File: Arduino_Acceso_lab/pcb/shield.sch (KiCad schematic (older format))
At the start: 34 parts, among them K1 RELAY_C, K2 RELAY_C, P1 Power, P10 Sensor1, P11 Sensor2, P12 Luz1, P13 Luz2, P2 Analog, P3 Digital, P4 Digital, P5 modulo esp8266, P6 fuente, P7 buzzer 1, P8 buzzer 2, P9 Timer RTC, Q1 2N2222, Q2 2N2222, U1 LM2576

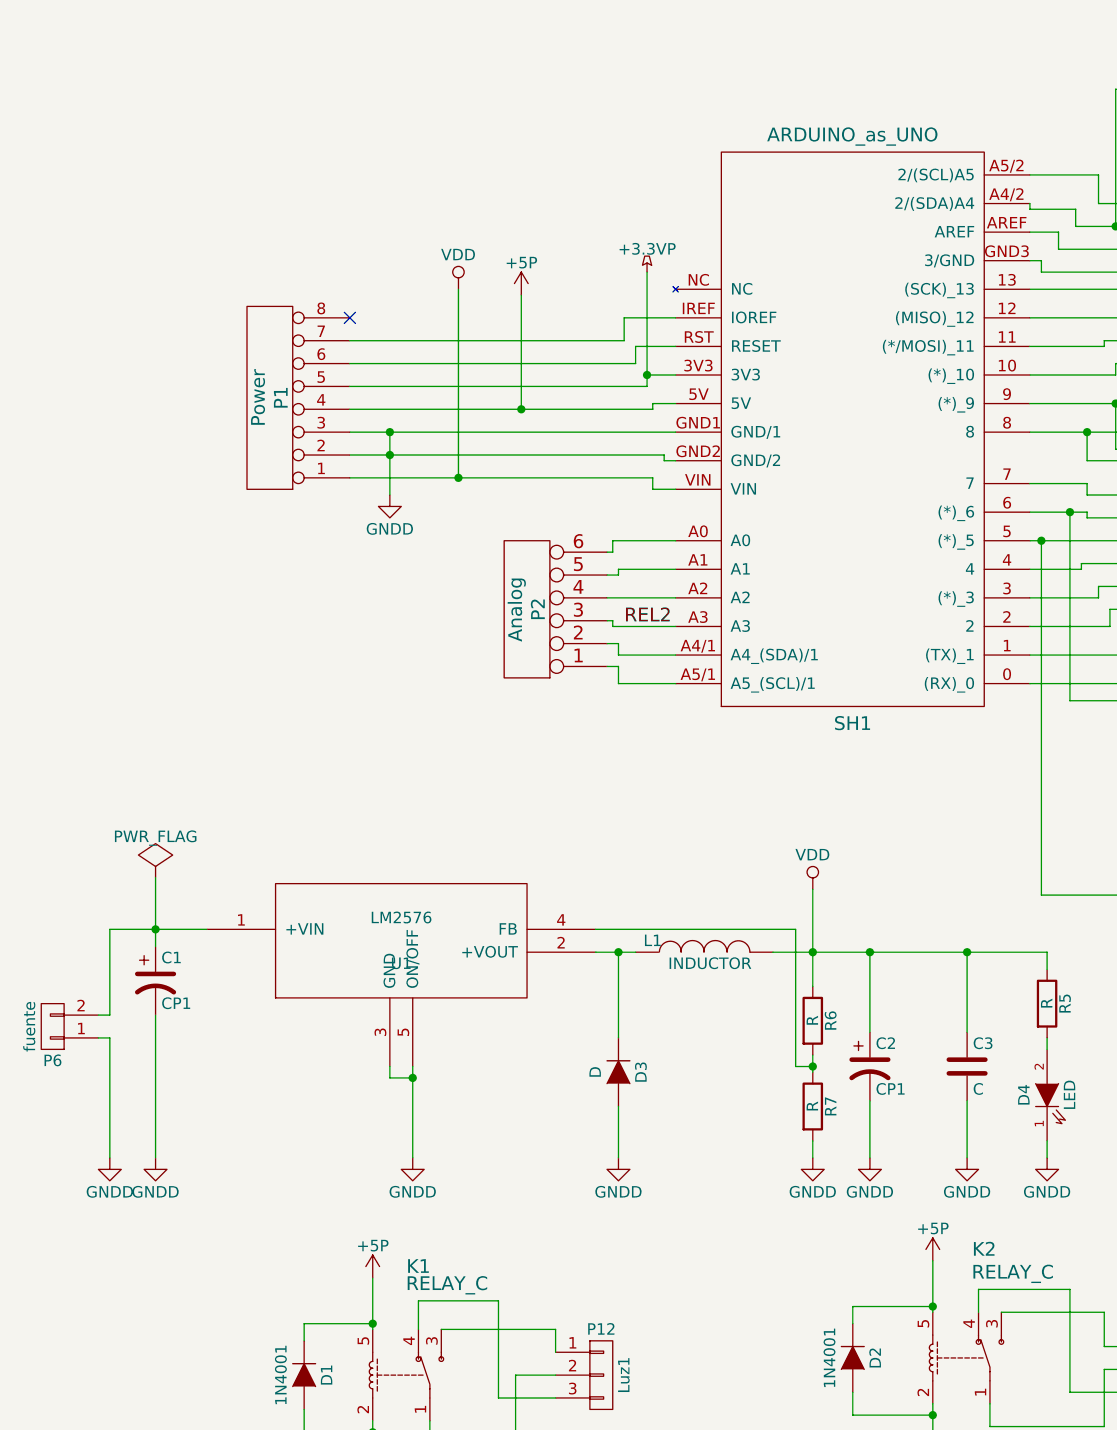
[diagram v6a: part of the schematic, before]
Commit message: Agrego avances en el PCB de Acceso Lab.
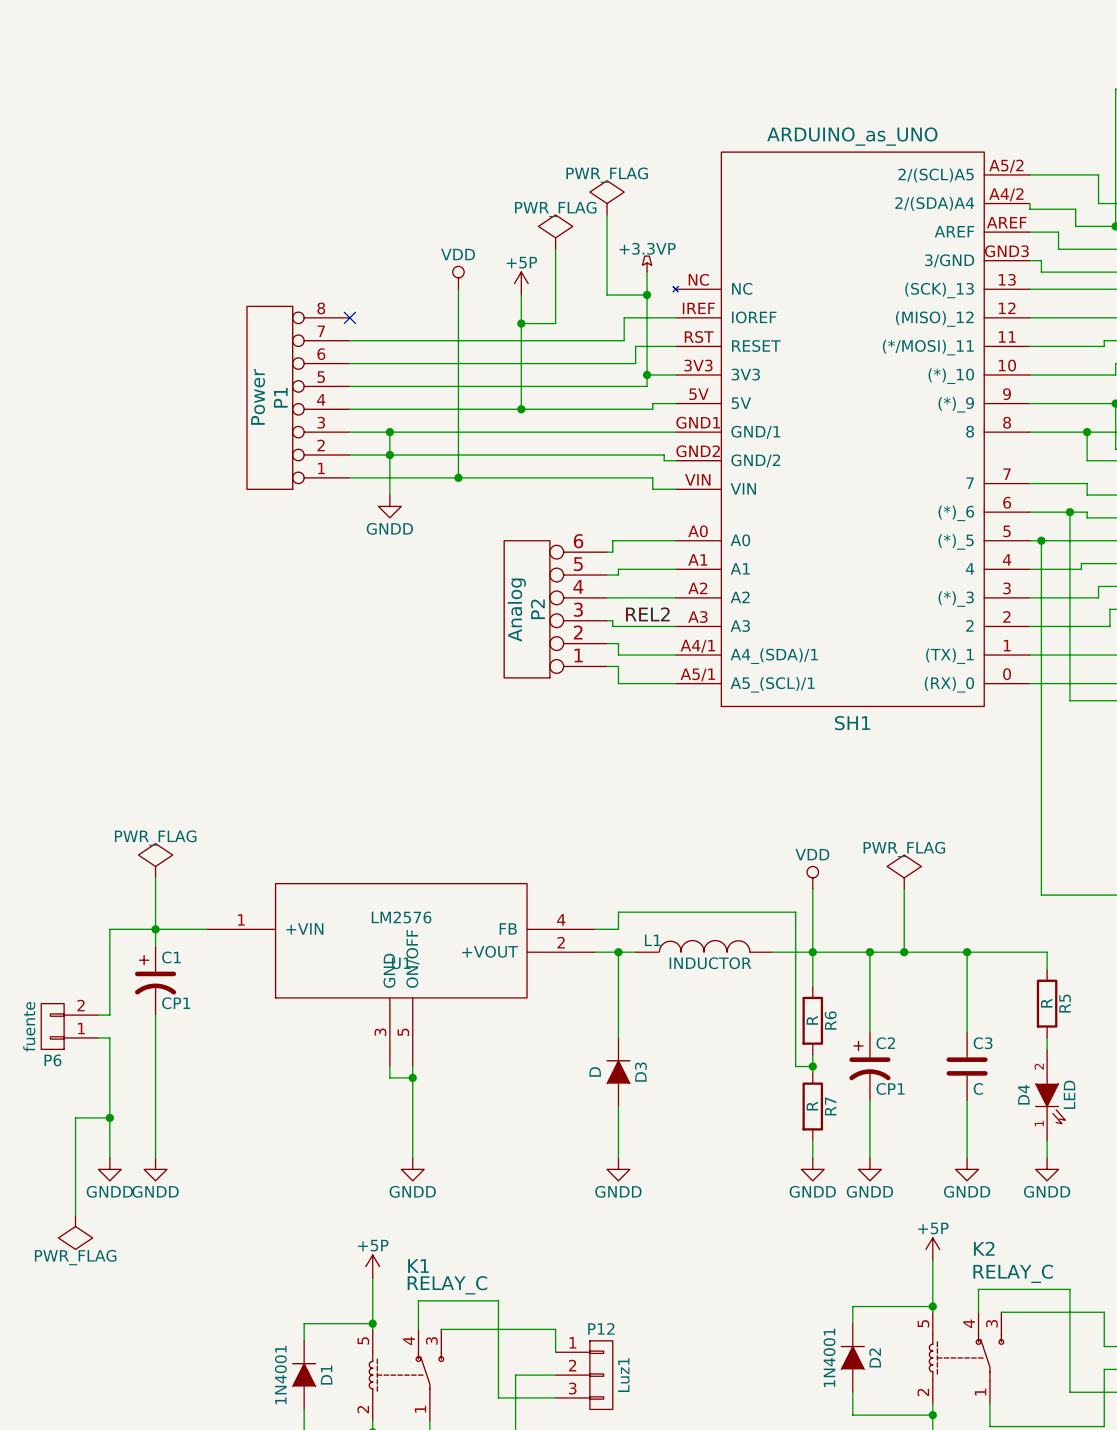
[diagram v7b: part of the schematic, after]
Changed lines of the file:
@@
 EESchema Schematic File Version 2
-LIBS:shield-rescue
 LIBS:power
 LIBS:shield-cache
@@
 Connection ~ 3100 4875
 Wire Wire Line
-	3000 4775 3875 4775
-Wire Wire Line
-	3875 4775 3875 5375
+	3875 4700 3875 5375
 Wire Wire Line
 	3950 4600 3950 5025
@@
 Connection ~ 1075 4775
 $Comp
-L PWR_FLAG #FLG03
+L PWR_FLAG #FLG01
 U 1 1 581D63A8
 P 1075 4550
-F 0 "#FLG03" H 1075 4645 50  0001 C CNN
+F 0 "#FLG01" H 1075 4645 50  0001 C CNN
 F 1 "PWR_FLAG" H 1075 4730 50  0000 C CNN
 F 2 "" H 1075 4550 50  0000 C CNN
@@
 	2225 6400 2225 6525
 $Comp
-L +5P #PWR04
+L +5P #PWR02
 U 1 1 581BA574
 P 7250 4800
-F 0 "#PWR04" H 7250 4650 50  0001 C CNN
+F 0 "#PWR02" H 7250 4650 50  0001 C CNN
 F 1 "+5P" H 7250 4940 50  0000 C CNN
 F 2 "" H 7250 4800 50  0000 C CNN
@@
 	7450 4800 7250 4800
 $Comp
-L +5P #PWR05
+L +5P #PWR03
 U 1 1 581BBB48
 P 6075 4750
-F 0 "#PWR05" H 6075 4600 50  0001 C CNN
+F 0 "#PWR03" H 6075 4600 50  0001 C CNN
 F 1 "+5P" H 6075 4890 50  0000 C CNN
 F 2 "" H 6075 4750 50  0000 C CNN
@@
 	6225 4750 6075 4750
 $Comp
-L +5P #PWR06
+L +5P #PWR04
 U 1 1 581BBE4F
 P 6700 1225
-F 0 "#PWR06" H 6700 1075 50  0001 C CNN
+F 0 "#PWR04" H 6700 1075 50  0001 C CNN
 F 1 "+5P" H 6700 1365 50  0000 C CNN
 F 2 "" H 6700 1225 50  0000 C CNN
@@
 	6700 1200 6700 1225
 $Comp
-L +5P #PWR07
+L +5P #PWR05
 U 1 1 581BC378
 P 2025 6300
-F 0 "#PWR07" H 2025 6150 50  0001 C CNN
+F 0 "#PWR05" H 2025 6150 50  0001 C CNN
 F 1 "+5P" H 2025 6440 50  0000 C CNN
 F 2 "" H 2025 6300 50  0000 C CNN
@@
 $EndComp
 $Comp
-L +5P #PWR08
+L +5P #PWR06
 U 1 1 581BC8F5
 P 4475 6225
-F 0 "#PWR08" H 4475 6075 50  0001 C CNN
+F 0 "#PWR06" H 4475 6075 50  0001 C CNN
 F 1 "+5P" H 4475 6365 50  0000 C CNN
 F 2 "" H 4475 6225 50  0000 C CNN
@@
 Connection ~ 4475 6425
 $Comp
-L +3.3VP #PWR09
+L +3.3VP #PWR07
 U 1 1 581BF2A8
 P 10225 5175
-F 0 "#PWR09" H 10375 5125 50  0001 C CNN
+F 0 "#PWR07" H 10375 5125 50  0001 C CNN
 F 1 "+3.3VP" H 10225 5275 50  0000 C CNN
 F 2 "" H 10225 5175 50  0000 C CNN
@@
 $EndComp
 $Comp
-L +3.3VP #PWR010
+L +3.3VP #PWR08
 U 1 1 581BF320
 P 3225 1900
-F 0 "#PWR010" H 3375 1850 50  0001 C CNN
+F 0 "#PWR08" H 3375 1850 50  0001 C CNN
 F 1 "+3.3VP" H 3225 2000 50  0000 C CNN
 F 2 "" H 3225 1900 50  0000 C CNN
@@
 $EndComp
 $Comp
-L GNDD #PWR011
+L GNDD #PWR09
 U 1 1 581C0200
 P 9050 5825
-F 0 "#PWR011" H 9050 5575 50  0001 C CNN
+F 0 "#PWR09" H 9050 5575 50  0001 C CNN
 F 1 "GNDD" H 9050 5675 50  0000 C CNN
 F 2 "" H 9050 5825 50  0000 C CNN
@@
 $EndComp
 $Comp
-L GNDD #PWR012
+L GNDD #PWR010
 U 1 1 581C02DE
 P 8700 4875
-F 0 "#PWR012" H 8700 4625 50  0001 C CNN
+F 0 "#PWR010" H 8700 4625 50  0001 C CNN
 F 1 "GNDD" H 8700 4725 50  0000 C CNN
 F 2 "" H 8700 4875 50  0000 C CNN
@@
 $EndComp
 $Comp
-L GNDD #PWR013
+L GNDD #PWR011
 U 1 1 581C0509
 P 7100 4325
-F 0 "#PWR013" H 7100 4075 50  0001 C CNN
+F 0 "#PWR011" H 7100 4075 50  0001 C CNN
 F 1 "GNDD" H 7100 4175 50  0000 C CNN
 F 2 "" H 7100 4325 50  0000 C CNN
@@
 $EndComp
 $Comp
-L GNDD #PWR014
+L GNDD #PWR012
 U 1 1 581C0844
 P 5850 4275
-F 0 "#PWR014" H 5850 4025 50  0001 C CNN
+F 0 "#PWR012" H 5850 4025 50  0001 C CNN
 F 1 "GNDD" H 5850 4125 50  0000 C CNN
 F 2 "" H 5850 4275 50  0000 C CNN
@@
 $EndComp
 $Comp
-L GNDD #PWR015
+L GNDD #PWR013
 U 1 1 581C0B3B
 P 4975 5775
-F 0 "#PWR015" H 4975 5525 50  0001 C CNN
+F 0 "#PWR013" H 4975 5525 50  0001 C CNN
 F 1 "GNDD" H 4975 5625 50  0000 C CNN
 F 2 "" H 4975 5775 50  0000 C CNN
@@
 $EndComp
 $Comp
-L GNDD #PWR016
+L GNDD #PWR014
 U 1 1 581C0EDC
 P 4625 5775
-F 0 "#PWR016" H 4625 5525 50  0001 C CNN
+F 0 "#PWR014" H 4625 5525 50  0001 C CNN
 F 1 "GNDD" H 4625 5625 50  0000 C CNN
 F 2 "" H 4625 5775 50  0000 C CNN
@@
 $EndComp
 $Comp
-L GNDD #PWR017
+L GNDD #PWR015
 U 1 1 581C0F4D
 P 4200 5775
-F 0 "#PWR017" H 4200 5525 50  0001 C CNN
+F 0 "#PWR015" H 4200 5525 50  0001 C CNN
 F 1 "GNDD" H 4200 5625 50  0000 C CNN
 F 2 "" H 4200 5775 50  0000 C CNN
@@
 $EndComp
 $Comp
-L GNDD #PWR018
+L GNDD #PWR016
 U 1 1 581C0FE0
 P 3950 5775
-F 0 "#PWR018" H 3950 5525 50  0001 C CNN
+F 0 "#PWR016" H 3950 5525 50  0001 C CNN
 F 1 "GNDD" H 3950 5625 50  0000 C CNN
 F 2 "" H 3950 5775 50  0000 C CNN
@@
 $EndComp
 $Comp
-L GNDD #PWR019
+L GNDD #PWR017
 U 1 1 581C1073
 P 3100 5775
-F 0 "#PWR019" H 3100 5525 50  0001 C CNN
+F 0 "#PWR017" H 3100 5525 50  0001 C CNN
 F 1 "GNDD" H 3100 5625 50  0000 C CNN
 F 2 "" H 3100 5775 50  0000 C CNN
@@
 $EndComp
 $Comp
-L GNDD #PWR020
+L GNDD #PWR018
 U 1 1 581C114A
 P 2200 5775
-F 0 "#PWR020" H 2200 5525 50  0001 C CNN
+F 0 "#PWR018" H 2200 5525 50  0001 C CNN
 F 1 "GNDD" H 2200 5625 50  0000 C CNN
 F 2 "" H 2200 5775 50  0000 C CNN
@@
 $EndComp
 $Comp
-L GNDD #PWR021
+L GNDD #PWR019
 U 1 1 581C12A9
 P 1075 5775
-F 0 "#PWR021" H 1075 5525 50  0001 C CNN
+F 0 "#PWR019" H 1075 5525 50  0001 C CNN
 F 1 "GNDD" H 1075 5625 50  0000 C CNN
 F 2 "" H 1075 5775 50  0000 C CNN
@@
 $EndComp
 $Comp
-L GNDD #PWR022
+L GNDD #PWR020
 U 1 1 581C135E
 P 875 5775
-F 0 "#PWR022" H 875 5525 50  0001 C CNN
+F 0 "#PWR020" H 875 5525 50  0001 C CNN
 F 1 "GNDD" H 875 5625 50  0000 C CNN
 F 2 "" H 875 5775 50  0000 C CNN
@@
 $EndComp
 $Comp
-L GNDD #PWR023
+L GNDD #PWR021
 U 1 1 581C13CF
 P 2025 7600
-F 0 "#PWR023" H 2025 7350 50  0001 C CNN
+F 0 "#PWR021" H 2025 7350 50  0001 C CNN
 F 1 "GNDD" H 2025 7450 50  0000 C CNN
 F 2 "" H 2025 7600 50  0000 C CNN
@@
 $EndComp
 $Comp
-L GNDD #PWR024
+L GNDD #PWR022
 U 1 1 581C15B6
 P 4475 7550
-F 0 "#PWR024" H 4475 7300 50  0001 C CNN
+F 0 "#PWR022" H 4475 7300 50  0001 C CNN
 F 1 "GNDD" H 4475 7400 50  0000 C CNN
 F 2 "" H 4475 7550 50  0000 C CNN
@@
 $EndComp
 $Comp
-L GNDD #PWR025
+L GNDD #PWR023
 U 1 1 581C16F3
 P 8500 2325
-F 0 "#PWR025" H 8500 2075 50  0001 C CNN
+F 0 "#PWR023" H 8500 2075 50  0001 C CNN
 F 1 "GNDD" H 8500 2175 50  0000 C CNN
 F 2 "" H 8500 2325 50  0000 C CNN
@@
 $EndComp
 $Comp
-L GNDD #PWR026
+L GNDD #PWR024
 U 1 1 581C1BA4
 P 8550 1650
-F 0 "#PWR026" H 8550 1400 50  0001 C CNN
+F 0 "#PWR024" H 8550 1400 50  0001 C CNN
 F 1 "GNDD" H 8550 1500 50  0000 C CNN
 F 2 "" H 8550 1650 50  0000 C CNN
@@
 $EndComp
 $Comp
-L GNDD #PWR027
+L GNDD #PWR025
 U 1 1 581C1D47
 P 6775 1625
-F 0 "#PWR027" H 6775 1375 50  0001 C CNN
+F 0 "#PWR025" H 6775 1375 50  0001 C CNN
 F 1 "GNDD" H 6775 1475 50  0000 C CNN
 F 2 "" H 6775 1625 50  0000 C CNN
@@
 $EndComp
 $Comp
-L GNDD #PWR028
+L GNDD #PWR026
 U 1 1 581C1EA6
 P 2100 2875
-F 0 "#PWR028" H 2100 2625 50  0001 C CNN
+F 0 "#PWR026" H 2100 2625 50  0001 C CNN
 F 1 "GNDD" H 2100 2725 50  0000 C CNN
 F 2 "" H 2100 2875 50  0000 C CNN
@@
 $EndComp
 $Comp
-L +5P #PWR029
+L +5P #PWR027
 U 1 1 581C3DC8
 P 2675 2000
-F 0 "#PWR029" H 2675 1850 50  0001 C CNN
+F 0 "#PWR027" H 2675 1850 50  0001 C CNN
 F 1 "+5P" H 2675 2140 50  0000 C CNN
 F 2 "" H 2675 2000 50  0000 C CNN
@@
 Connection ~ 2675 2500
 $Comp
-L VDD #PWR?
+L VDD #PWR028
 U 1 1 582A51D7
 P 2400 1975
-F 0 "#PWR?" H 2400 1825 50  0001 C CNN
+F 0 "#PWR028" H 2400 1825 50  0001 C CNN
 F 1 "VDD" H 2400 2125 50  0000 C CNN
 F 2 "" H 2400 1975 50  0000 C CNN
@@
 $EndComp
 $Comp
-L VDD #PWR?
+L VDD #PWR029
 U 1 1 582A5442
 P 3950 4600
-F 0 "#PWR?" H 3950 4450 50  0001 C CNN
+F 0 "#PWR029" H 3950 4450 50  0001 C CNN
 F 1 "VDD" H 3950 4750 50  0000 C CNN
 F 2 "" H 3950 4600 50  0000 C CNN
@@
 	1    0    0    -1
 $EndComp
+$Comp
+L PWR_FLAG #FLG030
+U 1 1 582A2DE6
+P 4350 4600
+F 0 "#FLG030" H 4350 4695 50  0001 C CNN
+F 1 "PWR_FLAG" H 4350 4780 50  0000 C CNN
+F 2 "" H 4350 4600 50  0000 C CNN
+F 3 "" H 4350 4600 50  0000 C CNN
+	1    4350 4600
+	1    0    0    -1
+$EndComp
+Wire Wire Line
+	4350 4600 4350 4875
+Connection ~ 4350 4875
+$Comp
+L PWR_FLAG #FLG031
+U 1 1 582A318B
+P 2825 1800
+F 0 "#FLG031" H 2825 1895 50  0001 C CNN
+F 1 "PWR_FLAG" H 2825 1980 50  0000 C CNN
+F 2 "" H 2825 1800 50  0000 C CNN
+F 3 "" H 2825 1800 50  0000 C CNN
+	1    2825 1800
+	1    0    0    -1
+$EndComp
+Wire Wire Line
+	2675 2125 2825 2125
+Wire Wire Line
+	2825 2125 2825 1800
+Connection ~ 2675 2125
+$Comp
+L PWR_FLAG #FLG032
+U 1 1 582A33B6
+P 3050 1650
+F 0 "#FLG032" H 3050 1745 50  0001 C CNN
+F 1 "PWR_FLAG" H 3050 1830 50  0000 C CNN
+F 2 "" H 3050 1650 50  0000 C CNN
+F 3 "" H 3050 1650 50  0000 C CNN
+	1    3050 1650
+	1    0    0    -1
+$EndComp
+Wire Wire Line
+	3050 2000 3225 2000
+Wire Wire Line
+	3050 2000 3050 1650
+Connection ~ 3225 2000
+$Comp
+L PWR_FLAG #FLG033
+U 1 1 582A36B2
+P 725 6025
+F 0 "#FLG033" H 725 6120 50  0001 C CNN
+F 1 "PWR_FLAG" H 725 6205 50  0000 C CNN
+F 2 "" H 725 6025 50  0000 C CNN
+F 3 "" H 725 6025 50  0000 C CNN
+	1    725  6025
+	-1   0    0    1
+$EndComp
+Wire Wire Line
+	725  6025 725  5600
+Wire Wire Line
+	725  5600 875  5600
+Connection ~ 875  5600
+Wire Wire Line
+	3000 4775 3100 4775
+Wire Wire Line
+	3100 4775 3100 4700
+Wire Wire Line
+	3100 4700 3875 4700
 $EndSCHEMATC
